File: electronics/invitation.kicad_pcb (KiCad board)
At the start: 2 copper layers, 86 x 57 mm, 51 parts, among them P1 USB Micro B, P10 Up Arrow, P11 Down Arrow, P2 Home btn, P3 Bottom Connections 1, P4 Left Arrow, P5 Right Arrow, P8 CONN_01X01, P9 CONN_01X02, U1 ATMEGA32U4-A, Y1 16 FA-238 Mhz

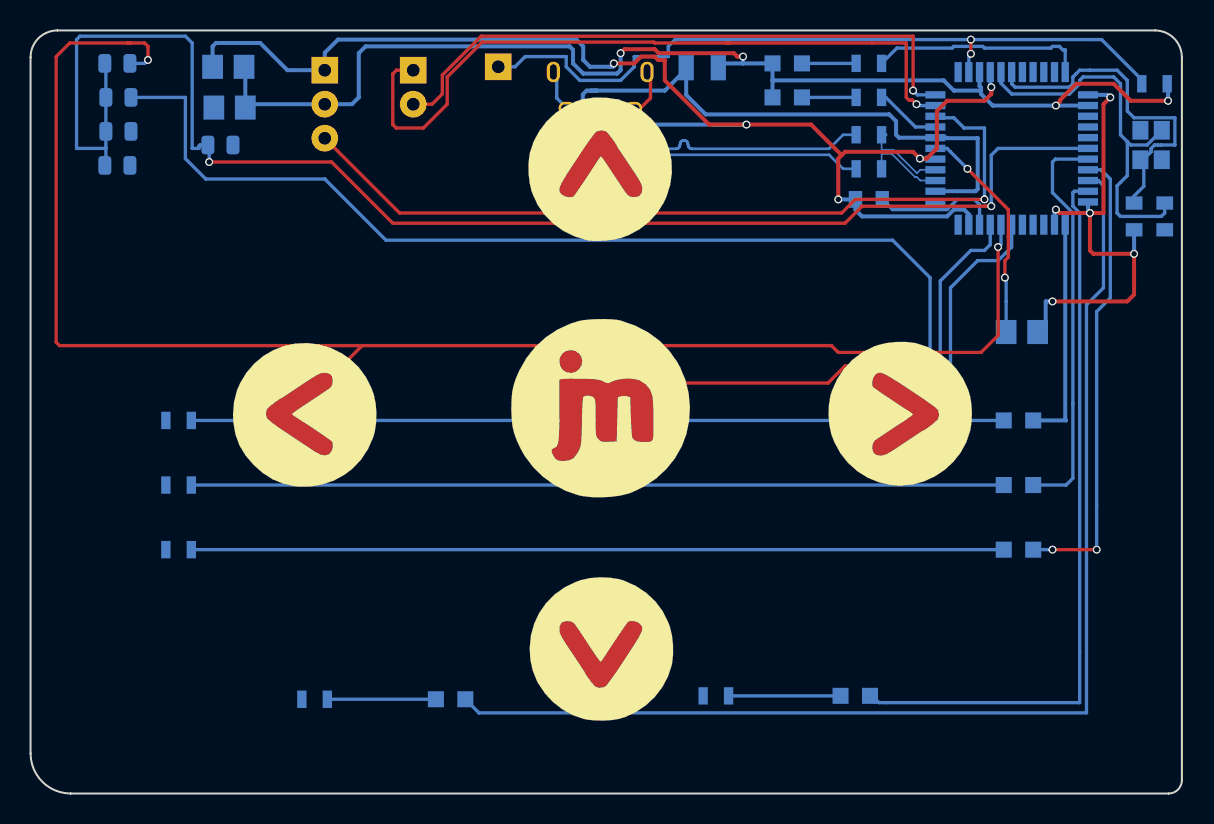
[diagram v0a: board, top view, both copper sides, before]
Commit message: Hero text fix + vr fix
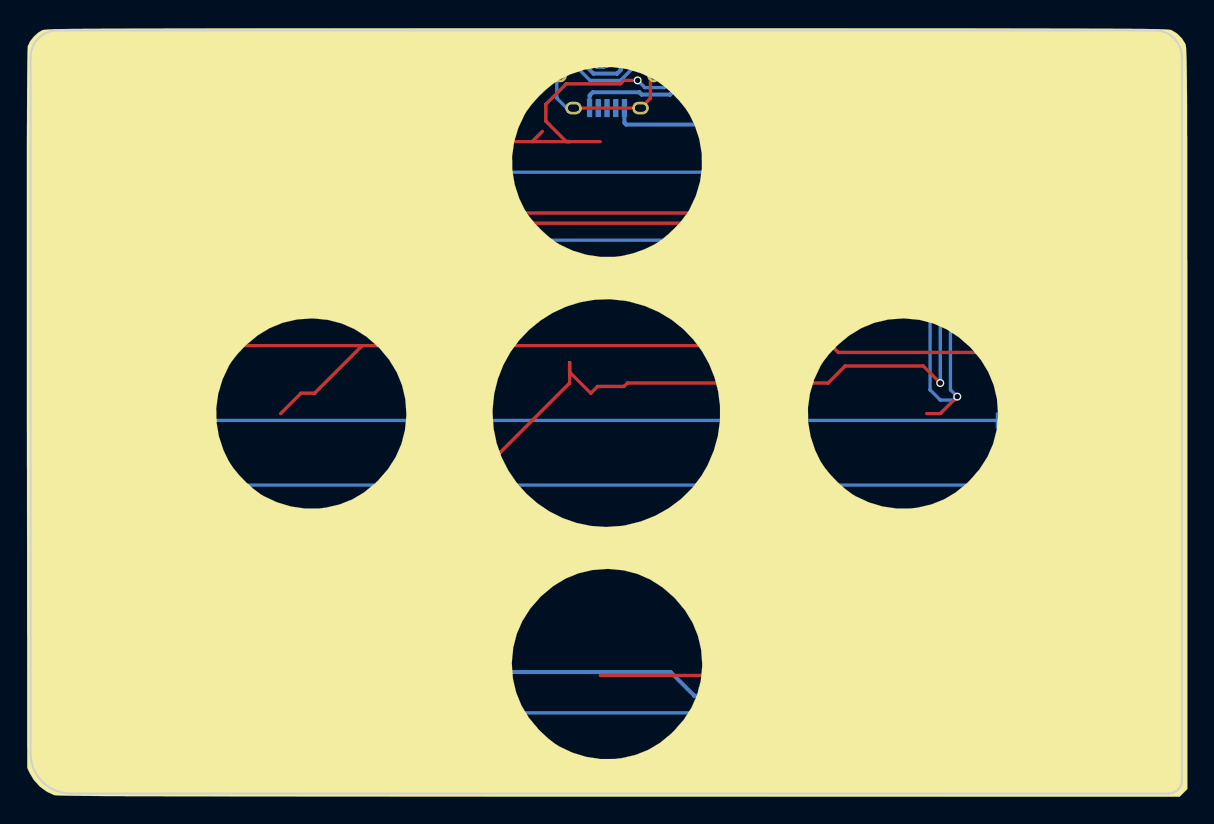
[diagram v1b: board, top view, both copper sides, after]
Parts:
- removed the G*** at (139.7, 99.8) (x2)
- removed the G*** at (161.8, 81.5) (x2)
- removed the G*** at (161.8, 117.3) (x2)
- removed the G*** at (161.8, 99.3) (x2)
- removed the G*** at (184.2, 99.8)
- removed P10: Up Arrow, newAssets:upArrow
- removed P11: Down Arrow, newAssets:downArrow
- removed P2: Home btn, newAssets:JMLogoFinal
- removed P4: Left Arrow, newAssets:leftArrow
- removed P5: Right Arrow, newAssets:rightArrow
- added G***: LOGO, newAssets:front-background, F.Cu at (162.3, 99.8)
- moved P1 0.51 mm to (162.3, 75.4)
- moved F1 0.44 mm to (169.9, 73.9)
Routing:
- net downArrSens: track 0.00 -> 187.6 mm, vias 0 -> 2
- net GND: track 137.3 -> 290.6 mm
- net upArrSens: track 0.00 -> 107.5 mm, vias 0 -> 2
- net homeSens: track 44.4 -> 145.6 mm, vias 1 -> 2
- net VCC: track 109.3 -> 147.3 mm, vias 4 -> 6
- net /Data+: track 23.1 -> 0.00 mm
- net /Data-: track 23.1 -> 0.00 mm
- net downArrBtn: track 109.6 -> 106.5 mm
- net Net-(C0-Pad1): track 16.6 -> 19.2 mm
- net rightArrSens: track 97.4 -> 96.1 mm
- net leftArrSens: track 119.3 -> 118.1 mm
- net SCLK: track 61.4 -> 60.8 mm
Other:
- board text added: "Connect this card to your PC with a USB cable Open in a web browser Tap the icons on this card’s reverse side"

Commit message: pub in progress
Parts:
- added G***: LOGO, newAssets:rightArrowSSFPaste, F.Cu at (184.4, 99.8)
- added G***: LOGO, newAssets:downArrowSSFPaste, F.Cu at (162.2, 118.5)
- added G***: LOGO, newAssets:JMLogoFinalSSFPaste, F.Cu at (162.2, 99.7)
- added G***: LOGO, newAssets:downArrowSSFMask, F.Cu at (162.2, 118.5)
- added G***: LOGO, newAssets:rightArrowSSFMask, F.Cu at (184.4, 99.8)
- added G***: LOGO, newAssets:leftArrowSSFMask, F.Cu at (140.2, 99.8)
- added G***: LOGO, newAssets:upArrowSSFMask, F.Cu at (162.4, 81.0)
- added G***: LOGO, newAssets:JMLogoFinalSSFMask, F.Cu at (162.2, 99.7)
- added G***: LOGO, newAssets:leftArrowSSFPaste, F.Cu at (140.2, 99.8)
- added G***: LOGO, newAssets:upArrowSSFPaste, F.Cu at (162.4, 81.0)
- added P10: Up Arrow, newAssets:upArrowSS, F.Cu at (162.4, 81.0)
- added P11: Down Arrow, newAssets:downArrowSS, F.Cu at (162.2, 118.5)
- added P2: Home btn, newAssets:JMLogoFinalSS, F.Cu at (162.2, 99.7)
- added P4: Left Arrow, newAssets:leftArrowSS, F.Cu at (140.2, 99.8)
- added P5: Right Arrow, newAssets:rightArrowSS, F.Cu at (184.4, 99.8)
- moved G*** 0.12 mm to (162.4, 99.7)

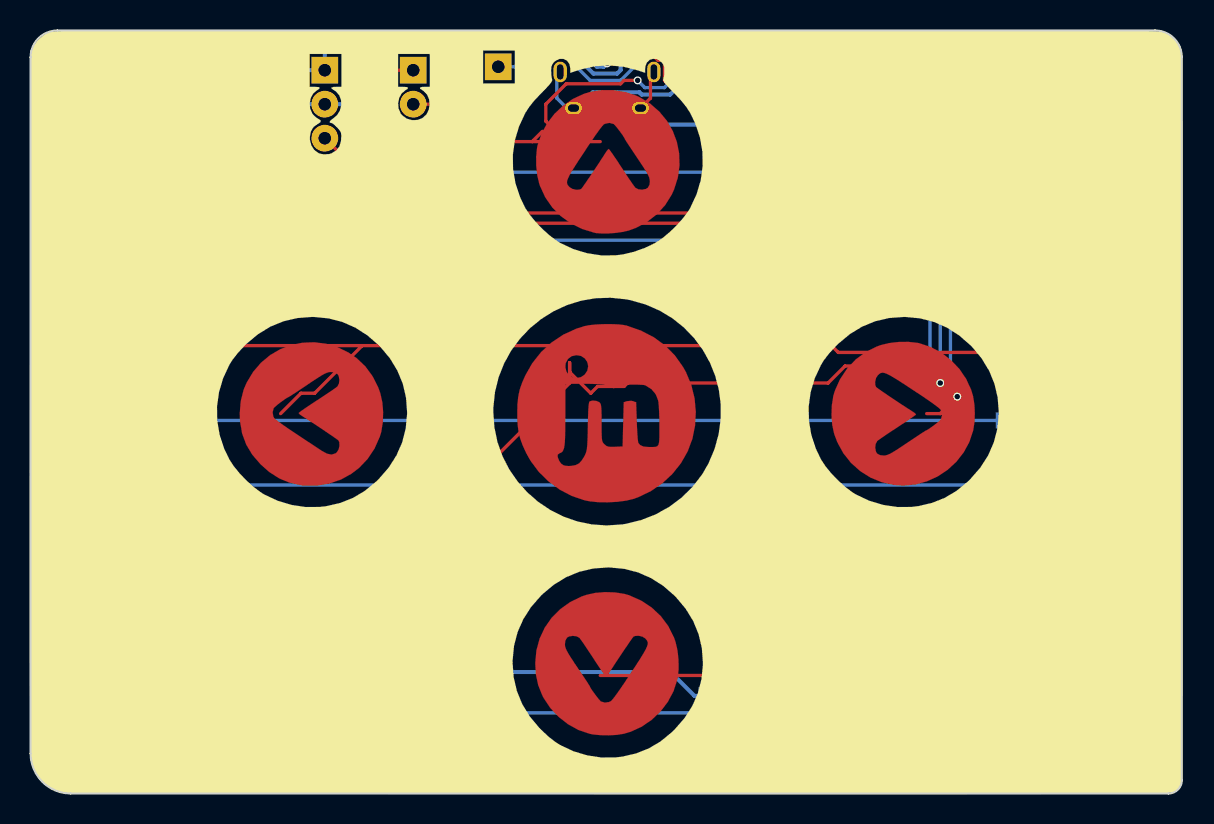
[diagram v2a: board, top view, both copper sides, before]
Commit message: Business card finished.
To do:
- Implement keyboard functionality to website
- Test Arduino code + electronics
- Get electronics card purchased
- Implement instructions for VR page on desktop
- Final check of website copy prior to getting biz cards reprinted
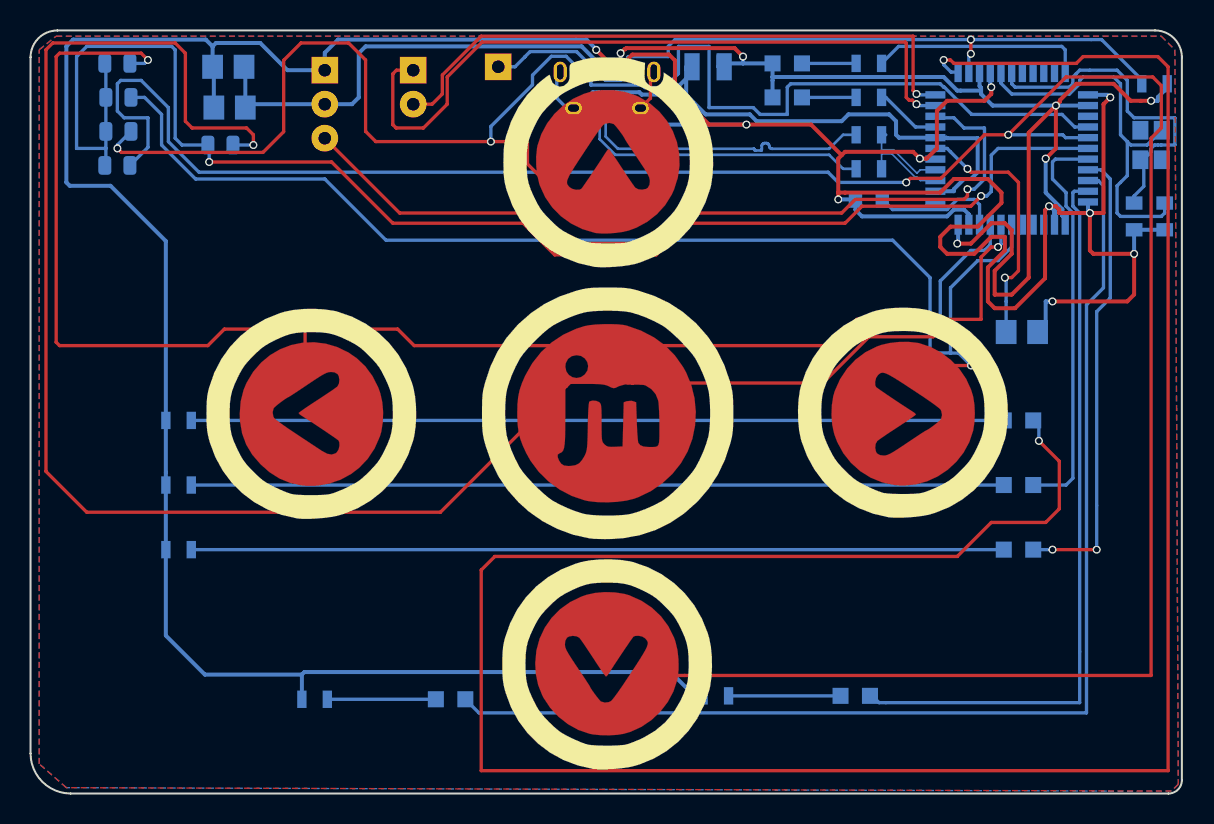
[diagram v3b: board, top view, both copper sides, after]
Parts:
- removed the G*** at (162.4, 99.7)
- added G***: LOGO, newAssets:front-background-two, F.Cu at (162.3, 99.8)
- R1, R2, R3, R4, R5: value 330 -> 47
- R6, R7: value 330 -> 82
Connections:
- D1 pad 2: VCC -> powerLED
- U1 pad 12: Net-(U1-Pad12) -> powerLED
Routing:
- net powerLED: track 0.00 -> 190.4 mm, vias 0 -> 2
- net /Data+: track 0.00 -> 22.4 mm
- net /Data-: track 0.00 -> 22.4 mm
- net VCC: track 147.3 -> 129.6 mm
- net upArrSens: track 107.5 -> 114.0 mm
- net homeSens: track 145.6 -> 141.3 mm
- net rightArrSens: track 96.1 -> 98.9 mm
- net downArrBtn: track 106.5 -> 108.5 mm
- net SCLK: track 60.8 -> 62.7 mm
- net downArrSens: track 187.6 -> 189.0 mm
- added copper zone on B.Cu, net GND
- added copper zone on F.Cu, net GND

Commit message: Completed WebVR animation of icon on scroll, V8 of PCB is in fabrication
To do:
- Implement webvr-polyfill for mobile
- More intuitive UX for webvr laptop experience
- Fix getOSVersion.js HOC (in Lincoln)
- Auto go-to webvr page on mobile if on iOS or android version .4 or higher
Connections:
- R11 pad 2: downArrBtn -> homeBtn
- R12 pad 2: downArrBtn -> homeBtn
- R13 pad 2: downArrBtn -> rightArrBtn
- R14 pad 2: downArrBtn -> rightArrBtn
- U1 pad 1: Net-(U1-Pad1) -> rightArrBtn
- U1 pad 25: Net-(U1-Pad25) -> downArrBtn
- U1 pad 28: downArrBtn -> homeBtn
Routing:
- net homeBtn: track 0.00 -> 189.2 mm, vias 0 -> 3
- net rightArrBtn: track 0.00 -> 72.2 mm, vias 0 -> 2
- net VCC: track 129.6 -> 139.2 mm
- net downArrSens: track 189.0 -> 182.7 mm, vias 2 -> 4
- net RESET: track 55.9 -> 61.7 mm
- net XTal2: track 28.8 -> 23.8 mm
- net GND: track 290.7 -> 295.4 mm
- net downArrBtn: track 108.5 -> 103.8 mm, vias 2 -> 4
- net XTal1: track 25.3 -> 21.4 mm
- net leftArrSens: track 118.3 -> 122.1 mm
- net upArrSens: track 114.0 -> 116.6 mm
- net USBVCC: track 42.7 -> 41.6 mm
- net Net-(C3-Pad1): track 9.56 -> 10.6 mm
- net MOSI: track 54.3 -> 55.0 mm
- net TXLED: track 16.0 -> 16.1 mm, vias 0 -> 2
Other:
- net class Data: clearance 0.1 -> 0.127
- net class Default: clearance 0 -> 0.127
- net class Power: clearance 0 -> 0.127
- rule trace_clearance: 0 -> 0.127

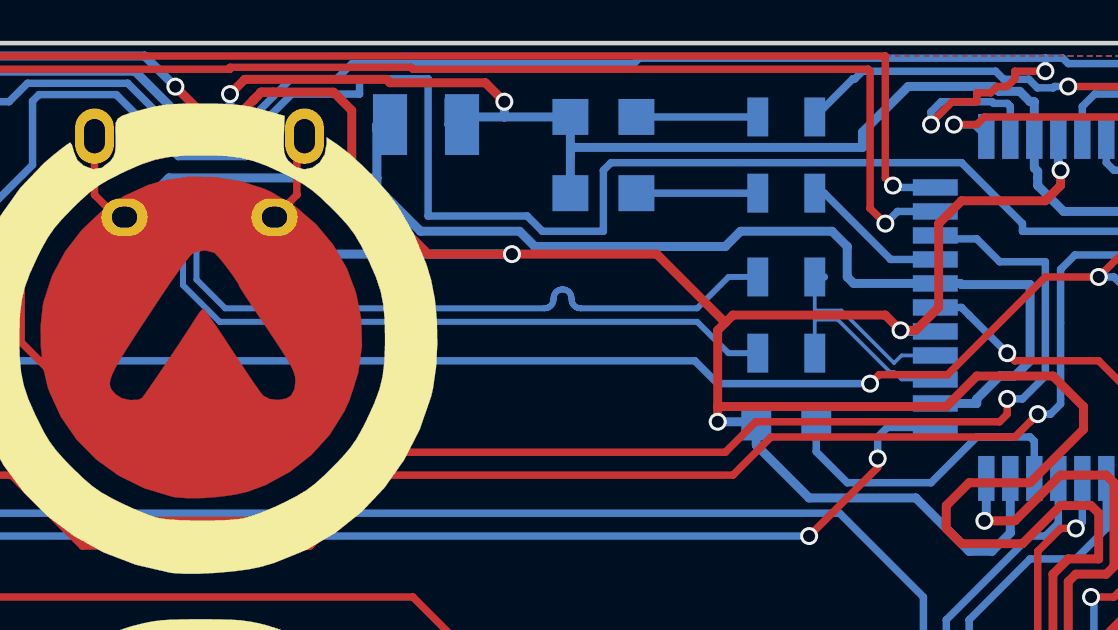
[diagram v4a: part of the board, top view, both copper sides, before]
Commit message: Updated electronics for Chinese suppliers (V10) and allowed device type detection for react360 device based experiences.
- To complete
1. Display appropriate VR content based on device
   - vertical mobile display message to turn phone horizontally
   - iOS chrome iframe not playing when clicked!
   - VR instructions and video not working
2. Create content for instruction page on headset webvr + mobile webvr + mobile + laptop
3. Finish coding for electronics card and test
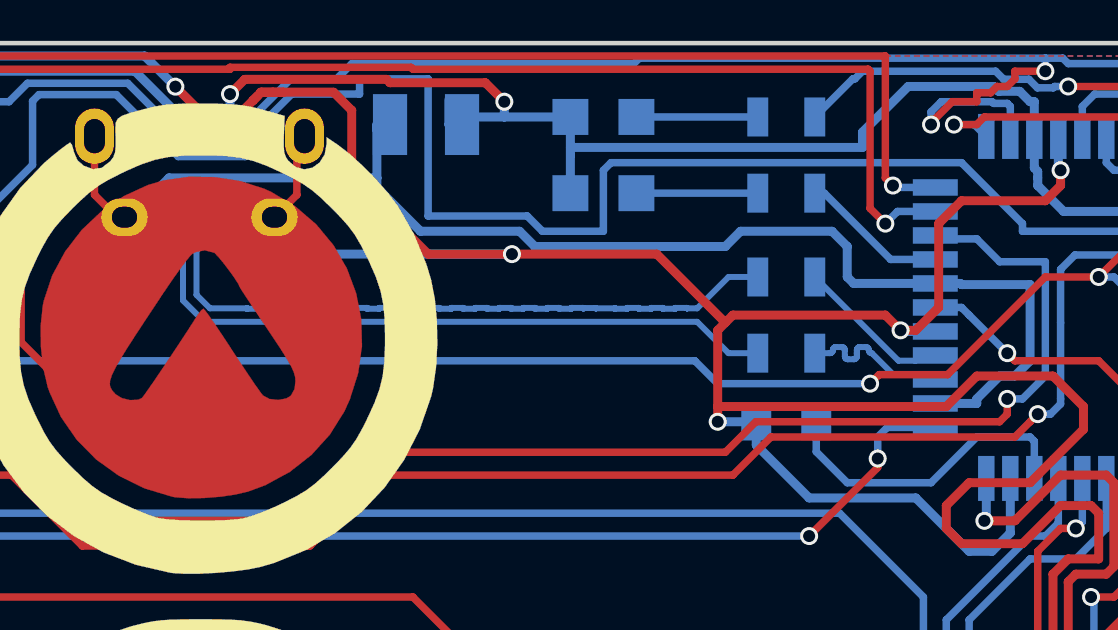
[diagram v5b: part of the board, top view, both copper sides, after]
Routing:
- net D+: track 6.28 -> 5.25 mm
- net D-: track 5.96 -> 5.25 mm
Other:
- net class Data: trace_width 0.12 -> 0.153
